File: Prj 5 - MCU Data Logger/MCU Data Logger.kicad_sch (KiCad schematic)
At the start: 0 parts

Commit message: +Custom components and loaded symbols
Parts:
- added C1, C2, C3, C4, C5, C6: C, symbol Device:C
- added D1, D2: LED, symbol Device:LED
- added H1, H2, H3, H4: MountingHole, symbol Mechanical:MountingHole
- added R1, R2, R3, R4, R5, R6, R7: R, symbol Device:R
- added U1: ATmega328-A, Package_QFP:TQFP-32_7x7mm_P0.8mm, symbol MCU_Microchip_ATmega:ATmega328-A
- added U2, U3: 24LC1025, symbol Memory_EEPROM:24LC1025
- added U4: DS1337S_, #download:SOIC127P600X175-8N, symbol #download:DS1337S_
- added Y1, Y2: Crystal, symbol Device:Crystal
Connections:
- new net: U1.21 (GND), U1.3 (GND), U1.5 (GND)
- new net: U1.4 (VCC), U1.6 (VCC)

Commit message: +hierarchical sheet
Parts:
- added BT1: Battery, symbol Device:Battery
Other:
- added sheet Connectors (connectors.kicad_sch)
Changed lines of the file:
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@@
+	)
+	(symbol
+		(lib_id "Device:Battery")
+		(at 90.17 58.42 0)
+		(unit 1)
+		(exclude_from_sim no)
+		(in_bom yes)
+		(on_board yes)
+		(dnp no)
+		(fields_autoplaced yes)
+		(property "Reference" "BT1"
+			(at 93.98 56.5784 0)
+			(effects
+				(font
+					(size 1.27 1.27)
+				)
+				(justify left)
+			)
+		)
+		(property "Value" "Battery"
+			(at 93.98 59.1184 0)
+			(effects
+				(font
+					(size 1.27 1.27)
+				)
+				(justify left)
+			)
+		)
+		(property "Footprint" ""
+			(at 90.17 56.896 90)
+			(effects
+				(font
+					(size 1.27 1.27)
+				)
+				(hide yes)
+			)
+		)
+		(property "Datasheet" "~"
+			(at 90.17 56.896 90)
+			(effects
+				(font
+					(size 1.27 1.27)
+				)
+				(hide yes)
+			)
+		)
+		(property "Description" "Multiple-cell battery"
+			(at 90.17 58.42 0)
+			(effects
+				(font
+					(size 1.27 1.27)
+				)
+				(hide yes)
+			)
+		)
+		(pin "1"
+		)
+		(pin "2"
+		)
+		(instances
+			(project ""
+				(path "/9e6b6f4b-c9cd-4b00-ba0a-ee2ed324f710"
+					(reference "BT1")
+					(unit 1)
+				)
+			)
+		)
 	)
 	(symbol
@@
 				)
 			)
+		)
+	)
+	(sheet
+		(at 248.92 19.05)
+		(size 20.32 29.21)
+		(fields_autoplaced yes)
+		(stroke
+			(width 0.1524)
+			(type solid)
+		)
+		(fill
+			(color 0 0 0 0.0000)
+		)
+		(property "Sheetname" "Connectors"
+			(at 248.92 18.3384 0)
+			(effects
+				(font
+					(size 1.27 1.27)
+				)
+				(justify left bottom)
+			)
+		)
+		(property "Sheetfile" "connectors.kicad_sch"
+			(at 248.92 48.8446 0)
+			(effects
+				(font
+					(size 1.27 1.27)
+				)
+				(justify left top)
+			)
+		)
+		(instances
+			(project "MCU Data Logger"
+				(path "/9e6b6f4b-c9cd-4b00-ba0a-ee2ed324f710"
+					(page "2")
+				)
+			)

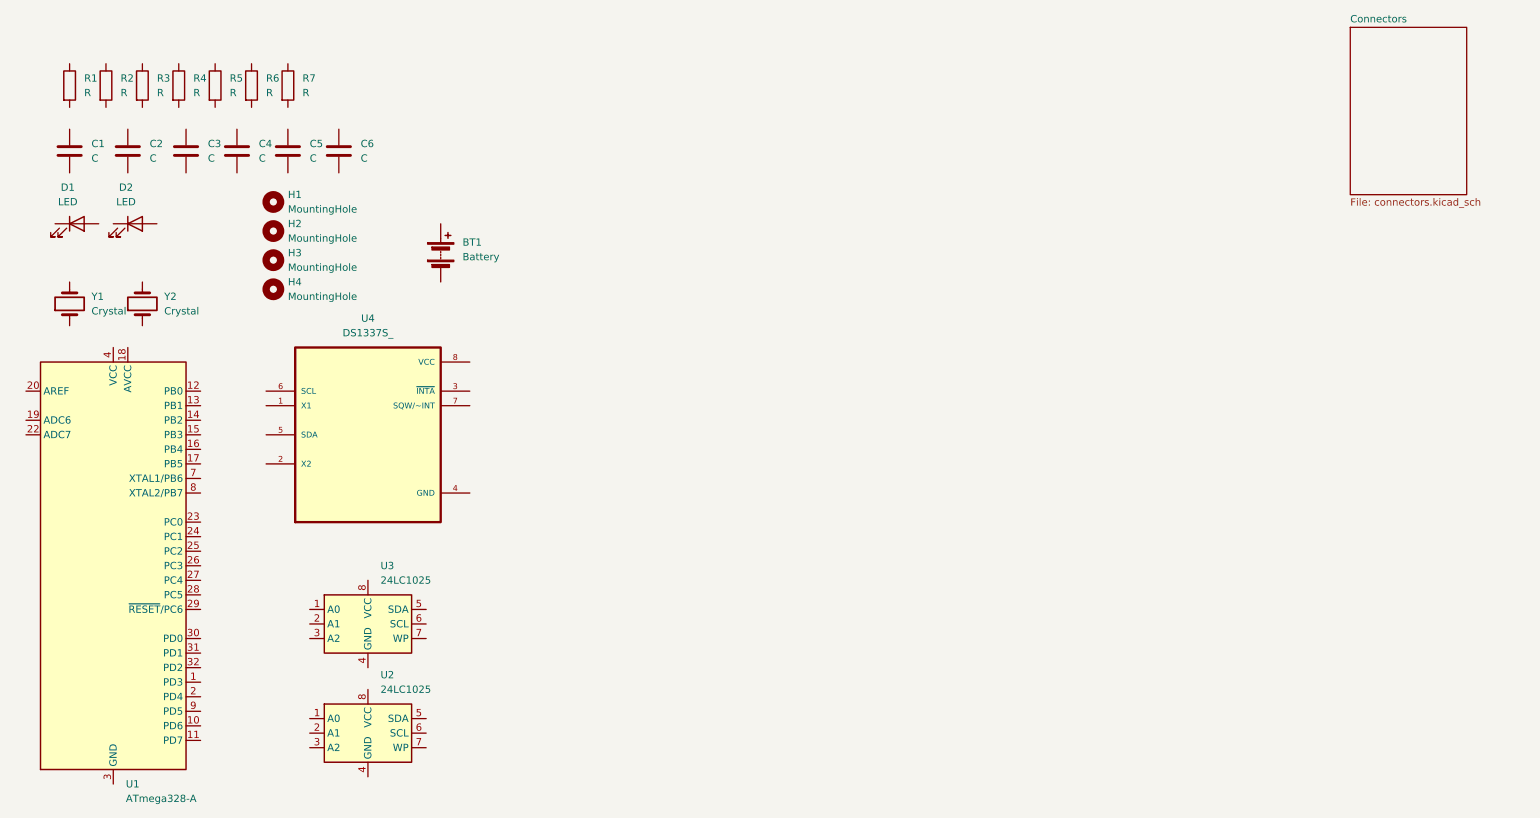
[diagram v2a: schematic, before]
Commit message: wired first main sheet
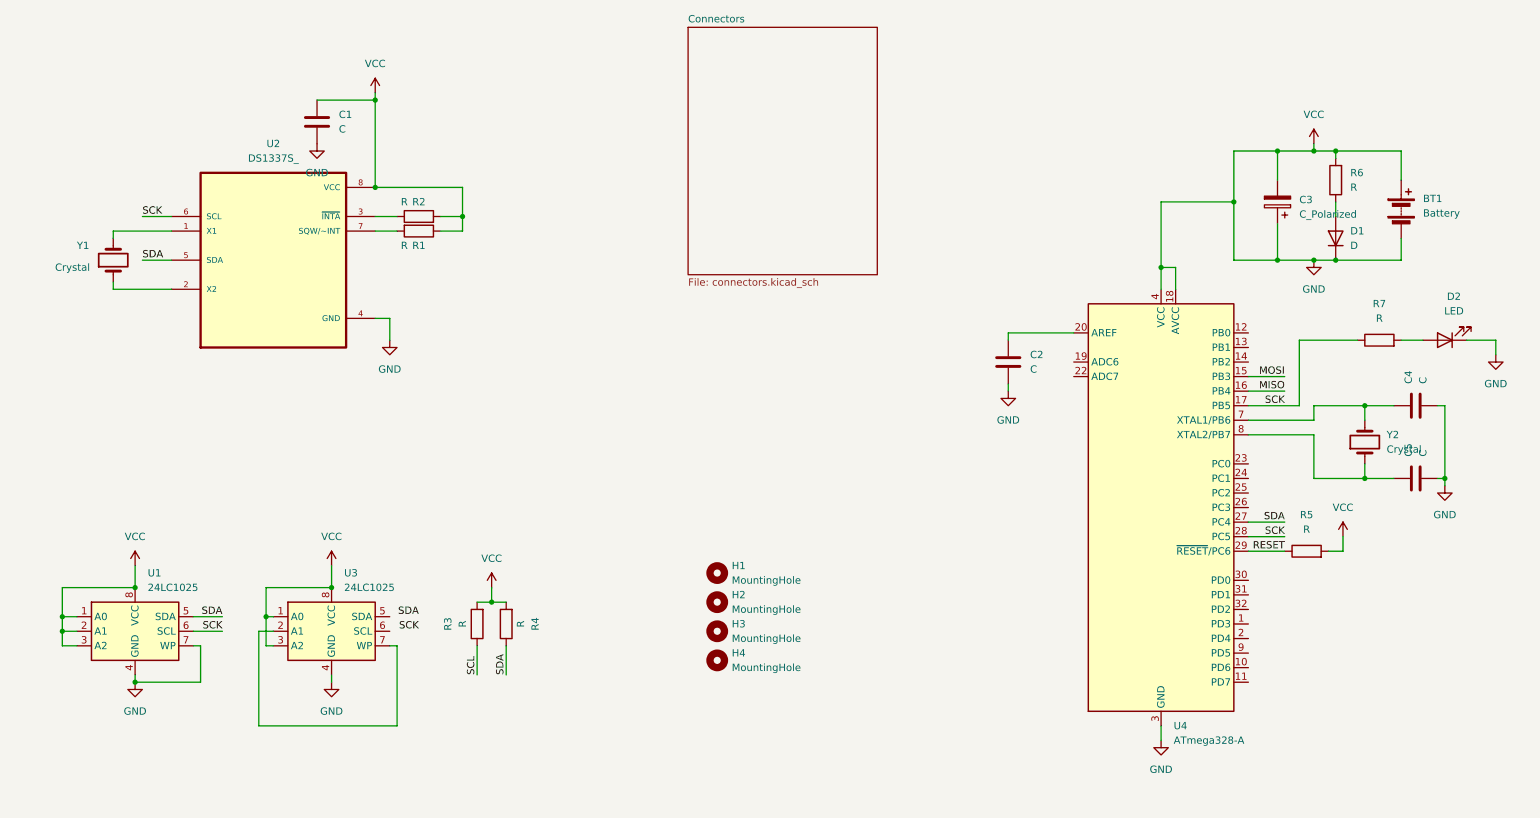
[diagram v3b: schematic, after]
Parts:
- removed C1, C6: C, symbol Device:C
- removed D1: LED, symbol Device:LED
- added C3: C_Polarized, symbol Device:C_Polarized
- added D1: D, symbol Device:D
- renumbered C5 to C1, C4 to C2, C3 to C4, C2 to C5, R2 to R1, R5 to R2, R6 to R3, R7 to R4, R1 to R5, R4 to R6, R3 to R7, U3 to U1, U4 to U2, U2 to U3, U1 to U4
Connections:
- net MOSI: now reaches U4.15 (PB3)
- net MISO: now reaches U4.16 (PB4)
- net SCK: now reaches U4.17 (PB5)
- net SCK: now also R7.1, U1.6 (SCL), U2.6 (SCL), U4.28 (PC5)
- net GND: now reaches U4.18 (AVCC)
- net GND: now also BT1.1 (+), BT1.2 (-), C1.1, C1.2, C2.2, C4.2, C5.2, D2.1 (K), R1.2, R2.1, R3.2, R4.2, R5.2, R6.2, U1.1 (A0), U1.2 (A1), U1.3 (A2), U1.4 (GND), U1.7 (WP), U1.8 (VCC), U2.4 (GND), U2.8 (VCC), U3.1 (A0), U3.3 (A2), U3.4 (GND), U3.8 (VCC), U4.21 (GND), U4.3 (GND), U4.4 (VCC), U4.5 (GND), U4.6 (VCC), C3.1, C3.2, D1.1 (K)
- net at U4.20 (AREF): now also C2.1
- net SDA: now reaches U4.27 (PC4)
- net SDA: now also R4.1, U1.5 (SDA), U2.5 (SDA)
- net RESET: now reaches U4.29 (~{RESET}/PC6)
- net RESET: now also R5.1
- net at U4.7 (XTAL1/PB6): now also C4.1, Y2.2
- net at U4.8 (XTAL2/PB7): now also C5.1, Y2.1
- net at R7.2: now also D2.2 (A)
- net at U2.1 (X1): now also Y1.2
- net at U2.2 (X2): now also Y1.1
- net at U2.3 (~{INTA}): now also R1.1
- net at U2.7 (SQW/~INT): now also R2.2
- net at R6.1: now also D1.2 (A)
- net at U3.2 (A1): now also U3.7 (WP)
- net SCL: now reaches R3.1
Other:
- moved on the sheet: BT1, C1, C2, C4, C5, D2, H1, H2, H3, H4, R1, R2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

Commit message: Complete wiring, ERC Clean
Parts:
- removed D1: D, symbol Device:D
- added D1: LED, symbol Device:LED
- C1, C2: value C -> 0.1u
- C3: value C_Polarized -> 100n
- C4, C5: value C -> 22p
- R1, R2: value R -> 10k
- R3, R4: value R -> 4.7K
- R5: value R -> 10K
- R6, R7: value R -> 330R
- U2: value DS1337S_ -> DS1337S+
- U4: value ATmega328-A -> ATmega328P
- Y1: value Crystal -> 32.768KHz
- Y2: value Crystal -> 16MHz
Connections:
- net SCL is gone; now on net SCK: R3.1
- net GND: now also U3.2 (A1), U3.7 (WP), D1.1 (K); no longer BT1.1 (+), C1.1, C3.1, R1.2, R2.1, R3.2, R4.2, R5.2, R6.2, U1.1 (A0), U1.2 (A1), U1.3 (A2), U1.8 (VCC), U2.8 (VCC), U3.1 (A0), U3.3 (A2), U3.8 (VCC), U4.18 (AVCC), U4.4 (VCC), U4.6 (VCC)
- net SCK: now also U3.6 (SCL)
- net SDA: now also U3.5 (SDA)
- net D3: now reaches U4.1 (PD3)
- net D6: now reaches U4.10 (PD6)
- net D7: now reaches U4.11 (PD7)
- net D8: now reaches U4.12 (PB0)
- net D4: now reaches U4.2 (PD4)
- net RX: now reaches U4.30 (PD0)
- net TX: now reaches U4.31 (PD1)
- net D2: now reaches U4.32 (PD2)
- net D5: now reaches U4.9 (PD5)
- net at R6.1: now also D1.2 (A)
- new net BVcc: BT1.1 (+), C1.1, C3.1, R1.2, R2.1, R3.2, R4.2, R5.2, R6.2, U1.1 (A0), U1.2 (A1), U1.3 (A2), U1.8 (VCC), U2.8 (VCC), U3.1 (A0), U3.3 (A2), U3.8 (VCC), U4.18 (AVCC), U4.4 (VCC), U4.6 (VCC)
- no-connect marks 0 -> 8
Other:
- sheet Connectors ports: added BVcc, D2, D3, D4, D5, D6, D7, D8, GND, MISO, MOSI, RESET, RX, SCK, SDA, TX; removed none
- note added: "Data Memory Bank"
- note added: "MCU and Power Supply"
- note added: "Mounting"
- note added: "Real Time Clock"
- moved on the sheet: C3, C5

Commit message: Associated footprints
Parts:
- BT1: footprint (none) -> Connector_PinHeader_2.54mm:PinHeader_1x02_P2.54mm_Vertical
- C1, C2, C3, C4, C5: footprint (none) -> Capacitor_SMD:C_0805_2012Metric
- D1, D2: footprint (none) -> LED_SMD:LED_0805_2012Metric
- H1, H2, H3, H4: footprint (none) -> MountingHole:MountingHole_2.1mm
- R1, R2, R3, R4, R5, R6, R7: footprint (none) -> Resistor_SMD:R_0805_2012Metric
- U1, U3: footprint (none) -> Package_SO:SOIC-8_5.23x5.23mm_P1.27mm
- Y1, Y2: footprint (none) -> Crystal:Crystal_SMD_5032-2Pin_5.0x3.2mm
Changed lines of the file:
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@@
 			)
 		)
-		(property "Footprint" ""
+		(property "Footprint" "MountingHole:MountingHole_2.1mm"
 			(at 138.43 129.54 0)
 			(effects
@@
 			)
 		)
-		(property "Footprint" ""
+		(property "Footprint" "Package_SO:SOIC-8_5.23x5.23mm_P1.27mm"
 			(at 36.83 124.46 0)
 			(effects
@@
 			)
 		)
-		(property "Footprint" ""
+		(property "Footprint" "Resistor_SMD:R_0805_2012Metric"
 			(at 254 75.438 90)
 			(effects
@@
 			)
 		)
-		(property "Footprint" ""
+		(property "Footprint" "MountingHole:MountingHole_2.1mm"
 			(at 138.43 124.46 0)
 			(effects
@@
 			)
 		)
-		(property "Footprint" ""
+		(property "Footprint" "Crystal:Crystal_SMD_5032-2Pin_5.0x3.2mm"
 			(at 33.02 59.69 0)
 			(effects
@@
 			)
 		)
-		(property "Footprint" ""
+		(property "Footprint" "Connector_PinHeader_2.54mm:PinHeader_1x02_P2.54mm_Vertical"
 			(at 257.81 49.276 90)
 			(effects
@@
 			)
 		)
-		(property "Footprint" ""
+		(property "Footprint" "Capacitor_SMD:C_0805_2012Metric"
 			(at 262.89 96.8248 0)
 			(effects
@@
 			)
 		)
-		(property "Footprint" ""
+		(property "Footprint" "Resistor_SMD:R_0805_2012Metric"
 			(at 103.378 123.19 90)
 			(effects
@@
 			)
 		)
-		(property "Footprint" ""
+		(property "Footprint" "LED_SMD:LED_0805_2012Metric"
 			(at 246.38 55.88 0)
 			(effects
@@
 			)
 		)
-		(property "Footprint" ""
+		(property "Footprint" "Capacitor_SMD:C_0805_2012Metric"
 			(at 237.1852 53.34 0)
 			(effects
@@
 			)
 		)
-		(property "Footprint" ""
+		(property "Footprint" "Resistor_SMD:R_0805_2012Metric"
 			(at 86.36 52.832 90)
 			(effects
@@
 			)
 		)
-		(property "Footprint" ""
+		(property "Footprint" "Resistor_SMD:R_0805_2012Metric"
 			(at 248.158 45.72 90)
 			(effects
@@
 			)
 		)
-		(property "Footprint" ""
+		(property "Footprint" "Package_SO:SOIC-8_5.23x5.23mm_P1.27mm"
 			(at 71.12 124.46 0)
 			(effects
@@
 			)
 		)
-		(property "Footprint" ""
+		(property "Footprint" "LED_SMD:LED_0805_2012Metric"
 			(at 265.43 73.66 0)
 			(effects
@@
 			)
 		)
-		(property "Footprint" ""
+		(property "Footprint" "Capacitor_SMD:C_0805_2012Metric"
 			(at 190.1952 81.28 0)
 			(effects
@@
 			)
 		)
-		(property "Footprint" ""
+		(property "Footprint" "Capacitor_SMD:C_0805_2012Metric"
 			(at 69.5452 39.37 0)
 			(effects
@@
 			)
 		)
-		(property "Footprint" ""
+		(property "Footprint" "Resistor_SMD:R_0805_2012Metric"
 			(at 98.298 123.19 90)
 			(effects
@@
 			)
 		)
-		(property "Footprint" ""
+		(property "Footprint" "MountingHole:MountingHole_2.1mm"
 			(at 138.43 119.38 0)
 			(effects
@@
 			)
 		)
-		(property "Footprint" ""
+		(property "Footprint" "Resistor_SMD:R_0805_2012Metric"
 			(at 86.36 53.848 90)
 			(effects
@@
 			)
 		)
-		(property "Footprint" ""
+		(property "Footprint" "Capacitor_SMD:C_0805_2012Metric"
 			(at 264.16 84.1248 0)
 			(effects
@@
 			)
 		)
-		(property "Footprint" ""
+		(property "Footprint" "Crystal:Crystal_SMD_5032-2Pin_5.0x3.2mm"
 			(at 251.46 91.44 0)
 			(effects
@@
 			)
 		)
-		(property "Footprint" ""
+		(property "Footprint" "MountingHole:MountingHole_2.1mm"
 			(at 138.43 114.3 0)
 			(effects
@@
 			)
 		)
-		(property "Footprint" ""
+		(property "Footprint" "Resistor_SMD:R_0805_2012Metric"
 			(at 241.3 112.268 90)
 			(effects

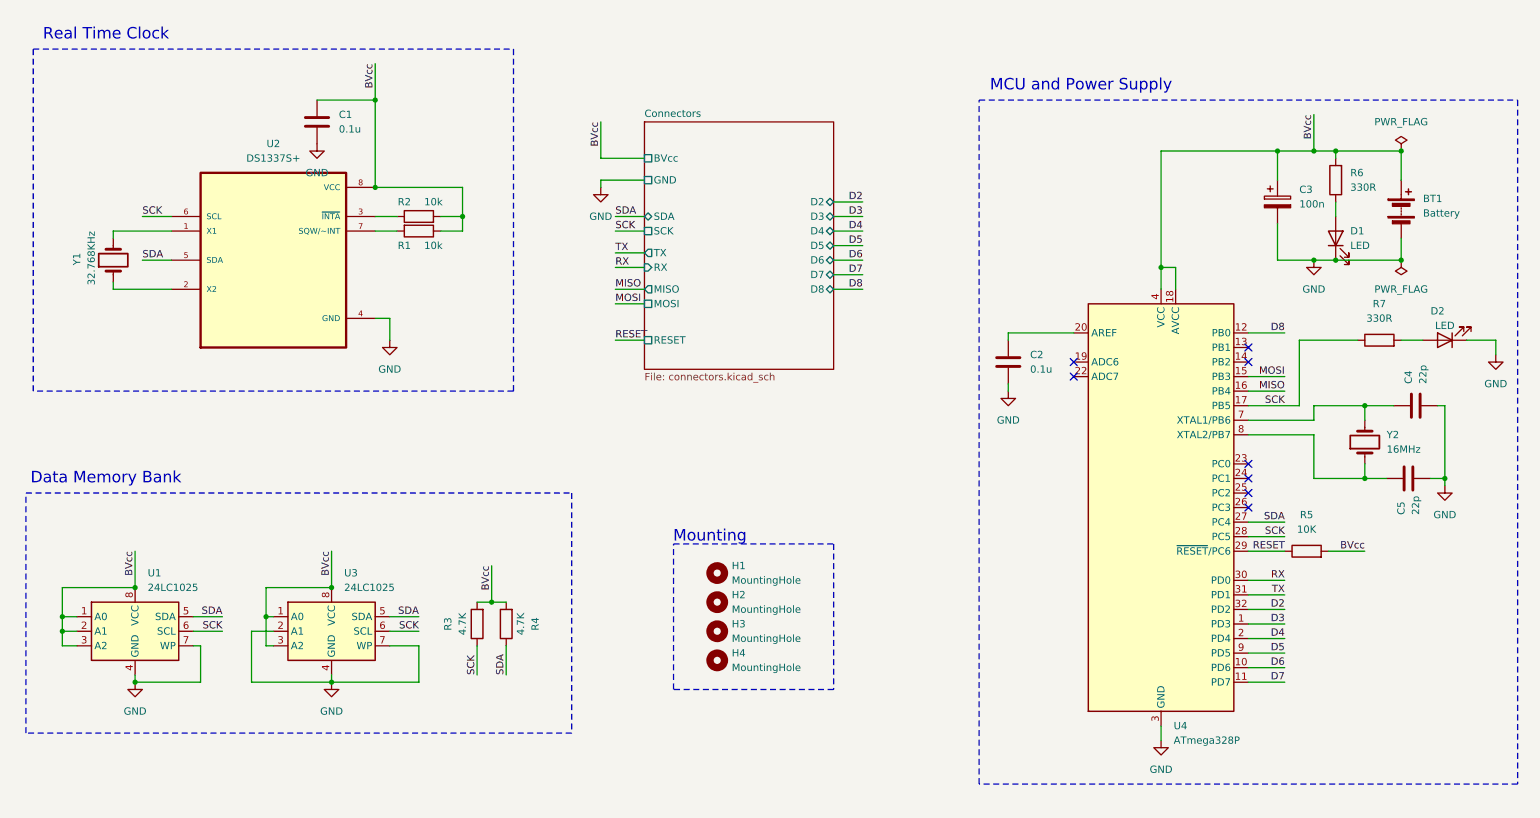
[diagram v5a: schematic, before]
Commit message: Separated SCL and SCK
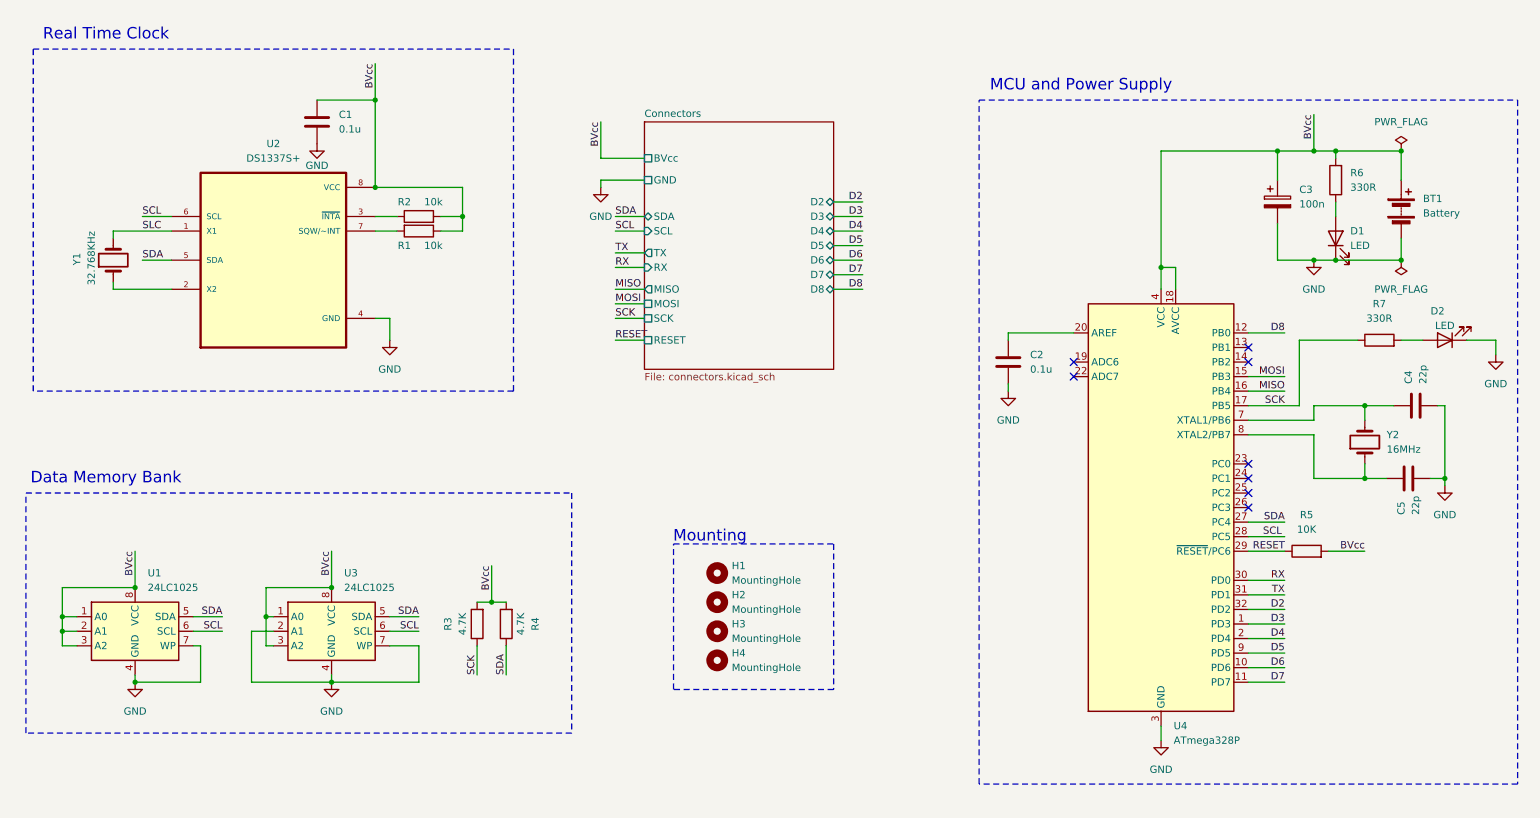
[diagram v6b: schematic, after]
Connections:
- net SCK: no longer U1.6 (SCL), U2.6 (SCL), U3.6 (SCL), U4.28 (PC5)
- net SLC: now reaches U2.1 (X1), Y1.2
- new net SCL: U1.6 (SCL), U2.6 (SCL), U3.6 (SCL), U4.28 (PC5)
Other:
- sheet Connectors ports: added SCL; removed none
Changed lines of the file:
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@@
 	(wire
 		(pts
+			(xy 120.65 54.61) (xy 125.73 54.61)
+		)
+		(stroke
+			(width 0)
+			(type default)
+		)
+	)
+	(wire
+		(pts
 			(xy 264.16 85.09) (xy 265.43 85.09)
 		)
@@
 	(wire
 		(pts
-			(xy 120.65 54.61) (xy 125.73 54.61)
+			(xy 120.65 69.85) (xy 125.73 69.85)
 		)
 		(stroke
@@
 		)
 	)
+	(label "SCL"
+		(at 233.68 107.95 0)
+		(fields_autoplaced yes)
+		(effects
+			(font
+				(size 1.27 1.27)
+			)
+			(justify left bottom)
+		)
+	)
 	(label "RESET"
 		(at 237.49 110.49 180)
@@
 	)
 	(label "SCK"
-		(at 120.65 54.61 0)
+		(at 120.65 69.85 0)
 		(fields_autoplaced yes)
 		(effects
@@
 		)
 	)
-	(label "SCK"
+	(label "SCL"
 		(at 38.1 52.07 0)
 		(fields_autoplaced yes)
@@
 		)
 	)
+	(label "SLC"
+		(at 38.1 54.61 0)
+		(fields_autoplaced yes)
+		(effects
+			(font
+				(size 1.27 1.27)
+			)
+			(justify left bottom)
+		)
+	)
 	(label "D3"
 		(at 163.83 52.07 180)
@@
 		)
 	)
-	(label "SCK"
-		(at 237.49 107.95 180)
-		(fields_autoplaced yes)
-		(effects
-			(font
-				(size 1.27 1.27)
-			)
-			(justify right bottom)
-		)
-	)
 	(label "D7"
 		(at 237.49 133.35 180)
@@
 		)
 	)
-	(label "SCK"
+	(label "SCL"
 		(at 52.07 124.46 180)
 		(fields_autoplaced yes)
@@
 		)
 	)
+	(label "SCL"
+		(at 120.65 54.61 0)
+		(fields_autoplaced yes)
+		(effects
+			(font
+				(size 1.27 1.27)
+			)
+			(justify left bottom)
+		)
+	)
 	(label "SDA"
 		(at 52.07 121.92 180)
@@
 		)
 	)
-	(label "SCK"
+	(label "SCL"
 		(at 86.36 124.46 180)
 		(fields_autoplaced yes)
@@
 		(on_board yes)
 		(dnp no)
-		(fields_autoplaced yes)
 		(property "Reference" "#PWR03"
 			(at 68.58 45.72 0)
@@
 		)
 		(property "Value" "GND"
-			(at 68.58 44.45 0)
+			(at 68.58 43.18 0)
 			(effects
 				(font
@@
 		)
 		(pin "SCK" passive
-			(at 125.73 54.61 180)
+			(at 125.73 69.85 180)
 			(effects
 				(font
@@
 			(effects
 				(font
+					(size 1.27 1.27)
+				)
+				(justify left)
+			)
+		)
+		(pin "SCL" input
+			(at 125.73 54.61 180)
+			(effects
+				(font
